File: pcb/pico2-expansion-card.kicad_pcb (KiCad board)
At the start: 2 copper layers, 26 x 30 mm, 39 parts, among them J3 Conn_01x04_Socket, J4 Conn_01x03_Socket, P1 USB_C_Plug_USB2.0, SW1 SW_Push, U2 RP2354A, U4 AP2127K-3.3, Y1 ABM8-272-T3

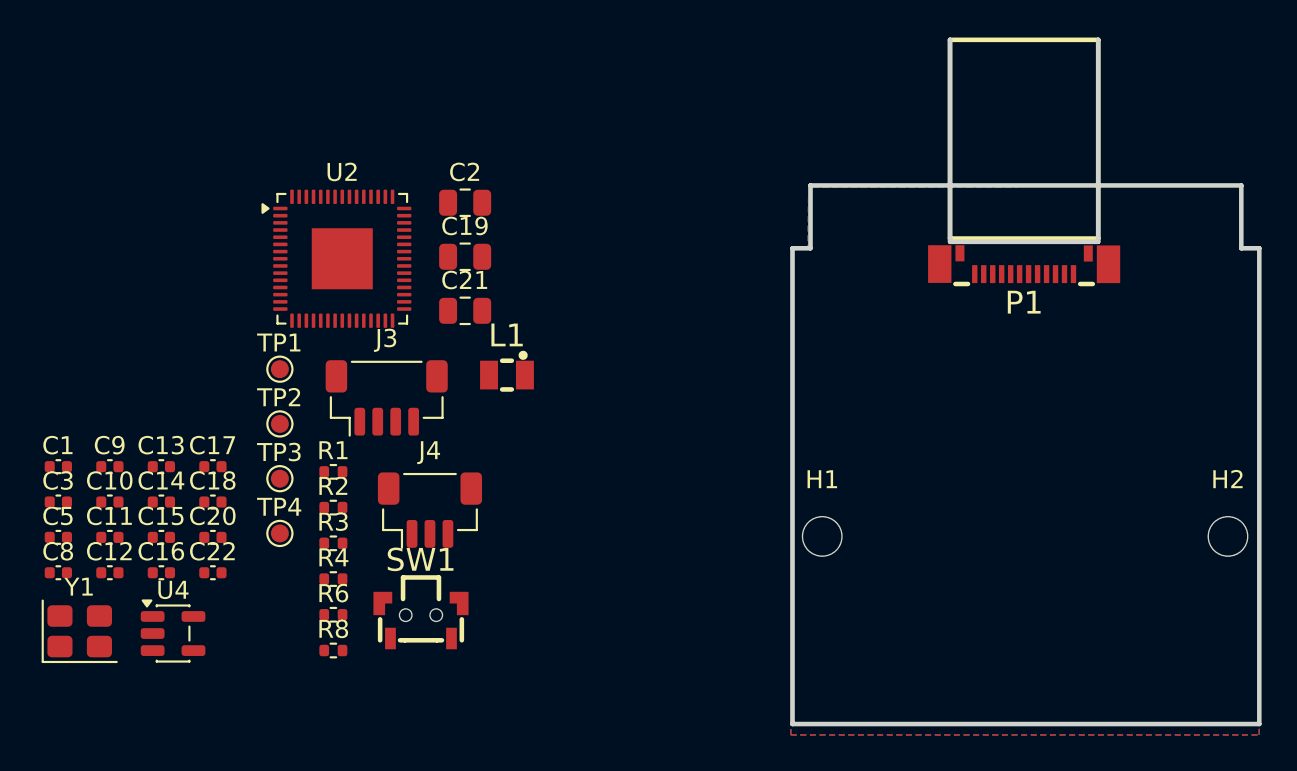
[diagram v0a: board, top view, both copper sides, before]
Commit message: edit schematic, change type-c, add single button bootsel reset, make pcb
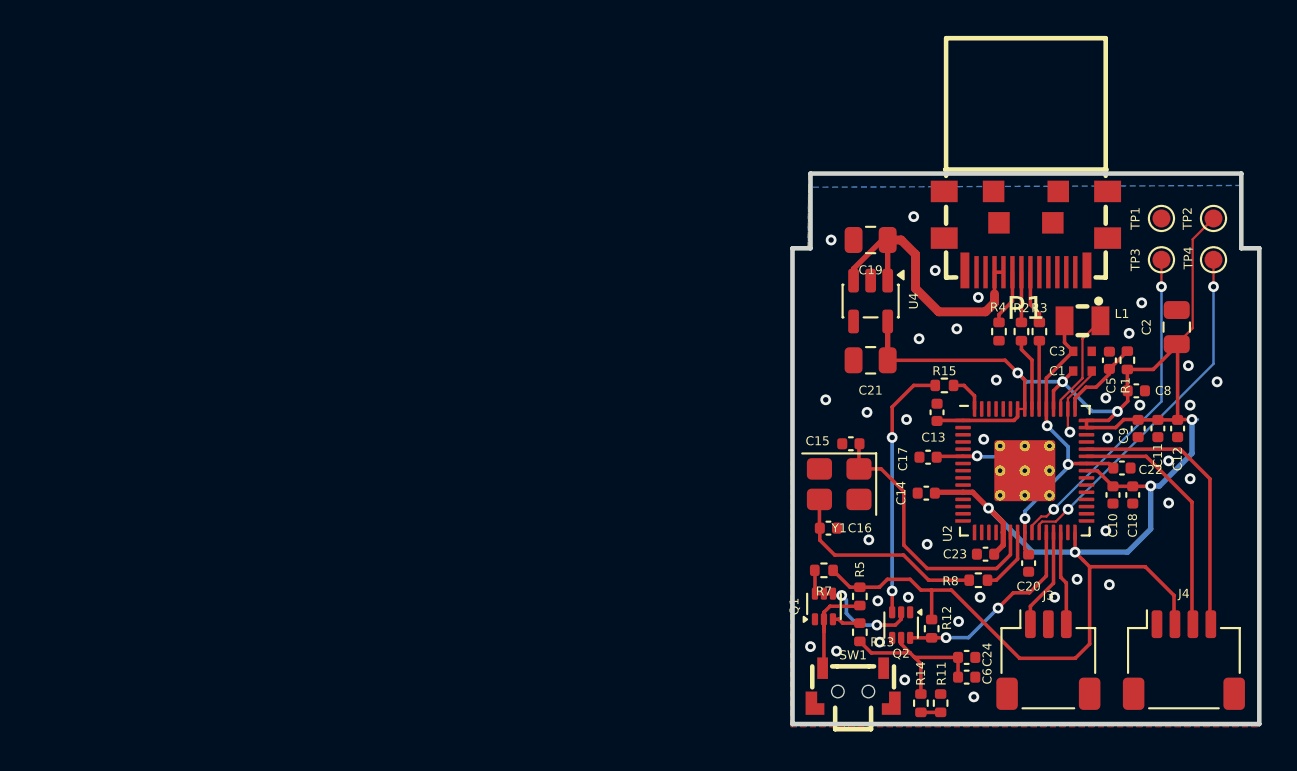
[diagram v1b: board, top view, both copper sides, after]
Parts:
- removed H1, H2: MountingHole, MountingHole:MountingHole_2.2mm_M2
- removed R6: 1k, Resistor_SMD:R_0402_1005Metric
- added C23: 100n, Capacitor_SMD:C_0402_1005Metric, F.Cu at (167.0, 91.5)
- added C24: 4u7, Capacitor_SMD:C_0402_1005Metric, F.Cu at (165.9, 97.2)
- added C6: 4u7, Capacitor_SMD:C_0402_1005Metric, F.Cu at (165.9, 98.3)
- added Q1: EM6K6, Package_TO_SOT_SMD:SOT-563, F.Cu at (158.0, 94.4)
- added Q2: EM6K6, Package_TO_SOT_SMD:SOT-563, F.Cu at (162.3, 95.5)
- added R11: 51K, Resistor_SMD:R_0402_1005Metric, F.Cu at (164.5, 99.8)
- added R12: 5K1, Resistor_SMD:R_0402_1005Metric, F.Cu at (164.0, 95.7)
- added R13: 51K, Resistor_SMD:R_0402_1005Metric, F.Cu at (160.0, 95.8)
- added R14: 51K, Resistor_SMD:R_0402_1005Metric, F.Cu at (163.4, 99.8)
- added R15: 1K, Resistor_SMD:R_0402_1005Metric, F.Cu at (164.7, 82.1)
- added R5: 5K1, Resistor_SMD:R_0402_1005Metric, F.Cu at (160.0, 93.8)
- added R7: 5K1, Resistor_SMD:R_0402_1005Metric, F.Cu at (158.0, 92.4)
- C1, C3: footprint Capacitor_SMD:C_0402_1005Metric -> pico2parts:C_0402_1005Metric_small_pads
- J3: renamed from J4; footprint Connector_JST:JST_SH_BM03B-SRSS-TB_1x03-1MP_P1.00mm_Vertical -> Connector_JST:JST_SH_SM03B-SRSS-TB_1x03-1MP_P1.00mm_Horizontal
- J4: renamed from J3; footprint Connector_JST:JST_SH_BM04B-SRSS-TB_1x04-1MP_P1.00mm_Vertical -> Connector_JST:JST_SH_SM04B-SRSS-TB_1x04-1MP_P1.00mm_Horizontal
- P1: value USB_C_Plug_USB2.0 -> ~; footprint pico2parts:USB-SMD_TC-002_1 -> pico2parts:USB-C-SMD_TYPE-C-31-G-10
- U2: footprint Package_DFN_QFN:QFN-60-1EP_7x7mm_P0.4mm_EP3.4x3.4mm -> pico2parts:RP2350-QFN-60-1EP_7x7_P0.4mm_EP3.4x3.4mm_ThermalVias
- moved C8 60.9 mm to (175.4, 82.4), turned to 180 degrees
- moved C12 60.0 mm to (177.7, 84.5), turned to 90 degrees
- moved C5 59.4 mm to (173.9, 80.7), turned to 90 degrees
- moved C11 58.7 mm to (176.6, 84.5), turned to 90 degrees
- moved C3 57.7 mm to (172.4, 80.2)
- moved C9 57.3 mm to (175.5, 84.5), turned to 90 degrees
- moved C1 57.3 mm to (172.4, 81.3)
- moved C10 55.9 mm to (174.1, 88.2), turned to 90 degrees
- moved TP4 54.2 mm to (179.7, 75.1), turned to 90 degrees
- moved TP2 53.2 mm to (179.7, 72.8), turned to 90 degrees
- moved C18 51.2 mm to (175.2, 88.2), turned to 90 degrees
- moved C22 51.0 mm to (174.6, 86.7)
- moved TP3 50.6 mm to (176.8, 75.1), turned to 90 degrees
- moved TP1 49.8 mm to (176.8, 72.8), turned to 90 degrees
- moved J4 46.7 mm to (178.1, 97.4)
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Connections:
- J3 pad 1: /GPIO4/TX -> /GPIO16/TX
- J3 pad 3: /GPIO5/RX -> /GPIO17/RX
- SW1 pad 2: /~{USB_BOOT} -> /SWITCH
- U2 pad 26: unconnected-(U2-RUN-Pad26) -> /nRST
- U2 pad 27: /GPIO16 -> /GPIO16/TX
- U2 pad 28: /GPIO17 -> /GPIO17/RX
- U2 pad 60: Net-(U2-~{QSPI_SS}) -> /~{USB_BOOT}
- U2 pad 7: /GPIO4/TX -> /GPIO4
- U2 pad 8: /GPIO5/RX -> /GPIO5
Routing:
- net +3.3V: track 0.00 -> 113.6 mm, vias 0 -> 7
- net +1V1: track 0.00 -> 25.8 mm, vias 0 -> 4
- net /SWDIO: track 0.00 -> 19.7 mm, vias 0 -> 2
- net /SWCLK: track 0.00 -> 18.4 mm, vias 0 -> 2
- net VBUS: track 0.00 -> 16.6 mm
- net /GPIO27/SCL: track 0.00 -> 15.7 mm
- net /XIN: track 0.00 -> 15.5 mm
- net Net-(Q2B-D): track 0.00 -> 14.3 mm, vias 0 -> 2
- net /GPIO26/SDA: track 0.00 -> 13.8 mm
- net Net-(C16-Pad1): track 0.00 -> 11.5 mm
- net /nRST: track 0.00 -> 11.4 mm, vias 0 -> 2
- net Net-(Q2B-G): track 0.00 -> 10.3 mm
- net Net-(Q1A-D): track 0.00 -> 7.94 mm, vias 0 -> 2
- net /SWITCH: track 0.00 -> 6.22 mm
- net /VREG_LX: track 0.00 -> 5.83 mm
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- added copper zone on B.Cu, net GND
- added copper zone on F.Cu, net GND
- removed copper zone on F.Cu, net +3.3V
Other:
- board size 26 x 30 mm -> 26 x 30.7 mm

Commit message: finish v0.1.0p prototype design
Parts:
- added H1: MountingHole, MountingHole:MountingHole_2.2mm_M2, F.Cu at (158.0, 82.1)
- added H1: MountingHole, MountingHole:MountingHole_2.2mm_M2, F.Cu at (180.4, 82.0)
- moved R13 4.22 mm to (164.0, 97.2)
- moved C21 2.91 mm to (163.4, 79.9), turned to -90 degrees
- moved R14 2.56 mm to (165.8, 98.9), turned to 0 degrees
- moved R5 1.95 mm to (160.0, 91.9), turned to 90 degrees
- moved R11 1.32 mm to (165.8, 100.0), turned to 180 degrees
- moved R12 0.96 mm to (164.7, 95.0)
- moved C24 0.72 mm to (165.8, 96.5)
- moved C6 0.72 mm to (165.8, 97.7)
- moved Q2 0.64 mm to (162.3, 94.8)
- moved C2 0.35 mm to (177.7, 78.5)
- moved C10 0.10 mm to (174.0, 88.2)
- moved C18 0.10 mm to (175.1, 88.2)
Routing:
- net +3.3V: track 113.6 -> 105.1 mm, vias 7 -> 8
- net Net-(Q1B-D): track 1.59 -> 6.62 mm
- net /SWITCH: track 6.22 -> 11.1 mm
- net Net-(Q2B-G): track 10.3 -> 8.13 mm
- net /XIN: track 15.5 -> 14.8 mm
- net Net-(Q2B-D): track 14.3 -> 13.7 mm
- net Net-(Q1A-D): track 7.94 -> 7.32 mm, vias 2 -> 0
- net /nRST: track 11.4 -> 11.1 mm, vias 2 -> 0
- net GND: vias 38 -> 32
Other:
- board size 26 x 30.7 mm -> 26 x 30.9 mm
- board text added: "License: CERN-OHL-S v2 Version: 0.1.0p (Prototype)"
- board text added: "PCB produced by:"
- board text added: "Pico2 Expansion Card"

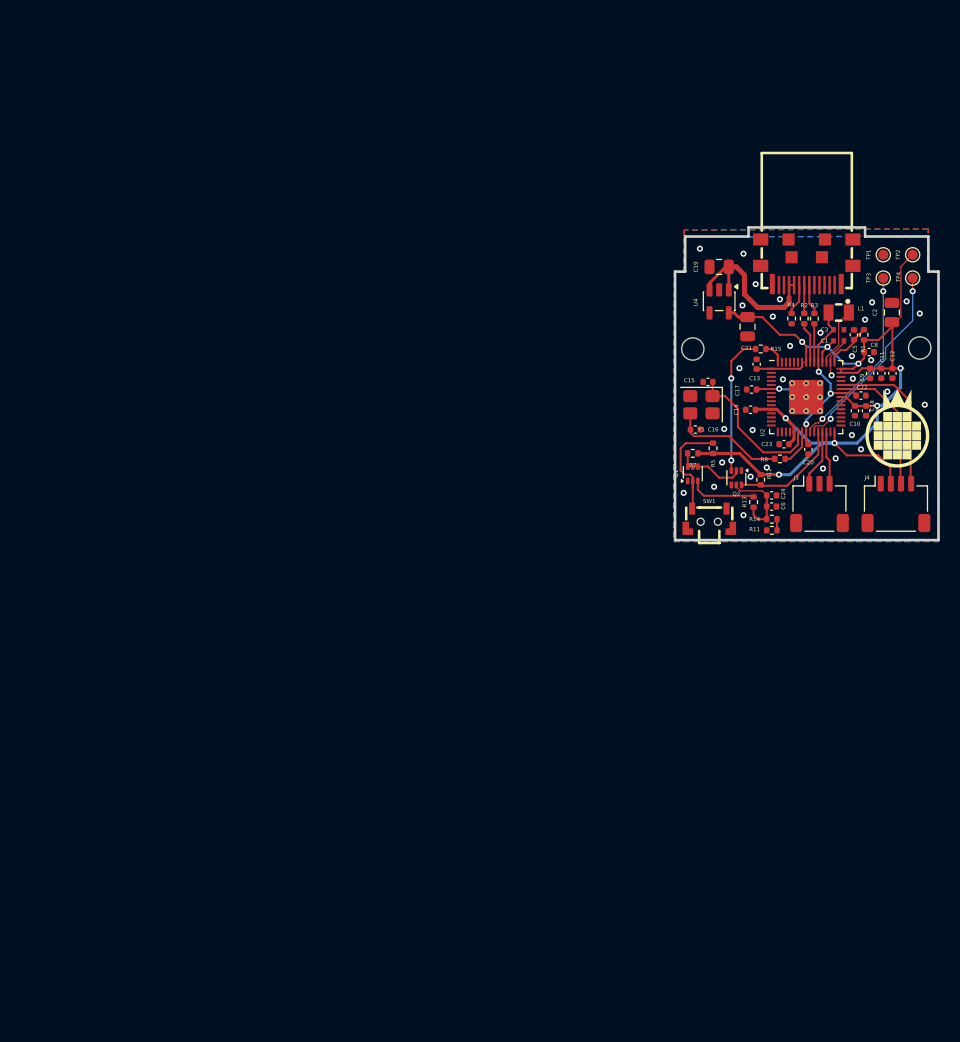
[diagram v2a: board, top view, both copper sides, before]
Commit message: minor cosmetic changes in schematics and footprints
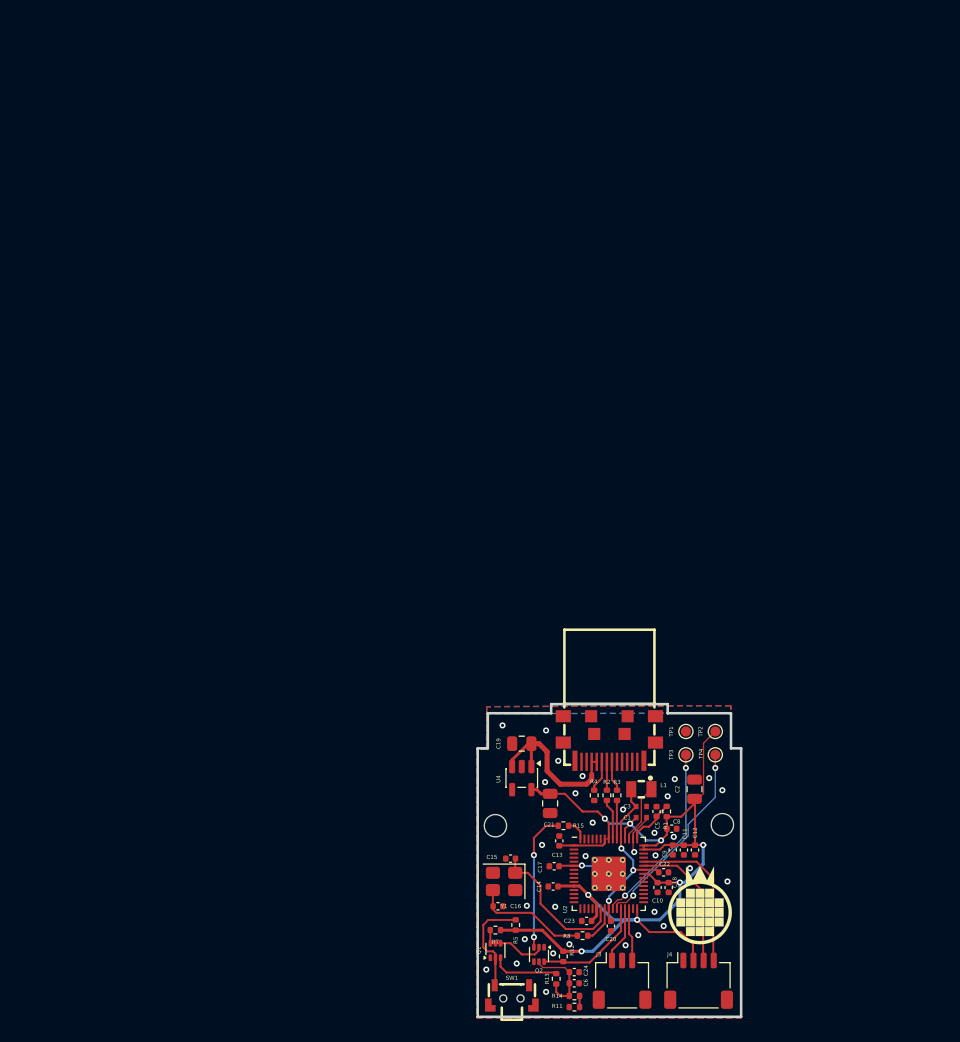
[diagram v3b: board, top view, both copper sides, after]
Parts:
- moved C13 50.9 mm to (144.8, 130.7)
- moved C17 50.9 mm to (144.3, 133.2)
- moved C20 50.9 mm to (149.9, 139.1)
- moved H1 50.9 mm to (160.9, 129.1)
- moved Q2 50.9 mm to (142.8, 141.9)
- moved R11 50.9 mm to (146.3, 147.1)
- moved R15 50.9 mm to (145.2, 129.2)
- moved TP3 50.9 mm to (157.3, 122.2)
- moved C11 50.9 mm to (157.1, 131.6)
- moved C12 50.9 mm to (158.2, 131.6)
- moved C14 50.9 mm to (144.2, 135.2)
- moved C15 50.9 mm to (140.0, 132.4)
- moved C23 50.9 mm to (147.5, 138.6)
- moved C9 50.9 mm to (156.0, 131.6)
- moved H1 50.9 mm to (138.5, 129.2)
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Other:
- board text added: "riscfruit.com"

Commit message: gerber and centroid
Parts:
- moved J3 0.06 mm to (151.0, 144.5)
- moved J4 0.06 mm to (158.6, 144.5)
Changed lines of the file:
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@@
 	(footprint "Connector_JST:JST_SH_SM03B-SRSS-TB_1x03-1MP_P1.00mm_Horizontal"
 		(layer "F.Cu")
-		(at 151.02 144.45)
+		(at 151.03 144.505)
 		(descr "JST SH series connector, SM03B-SRSS-TB (http://www.jst-mfg.com/product/pdf/eng/eSH.pdf)")
 		(tags "connector JST SH horizontal")
@@
 	(footprint "pico2parts:BUTTON-SW-SMD_2P-TS24CA"
 		(layer "F.Cu")
-		(at 140.145 145.875 180)
+		(at 140.145 145.905 180)
 		(property "Reference" "SW1"
 			(at 0.00005 1.7 0)
@@
 			(polygon
 				(pts
-					(xy 140.5516 144.8512) (xy 140.5506 145.0511) (xy 139.7504 145.0502) (xy 139.7497 144.8505) (xy 138.6497 144.8505)
-					(xy 138.6497 144.7505) (xy 138.2508 144.7503) (xy 138.2505 144.8501) (xy 137.8707 144.8476) (xy 137.8703 147.1494)
-					(xy 138.2484 147.1519) (xy 138.2691 147.3511) (xy 138.5301 147.3501) (xy 138.5505 147.15) (xy 139.0182 147.1525)
-					(xy 139.0067 148.427) (xy 141.2689 148.4272) (xy 141.2732 147.2288) (xy 142.4249 147.2263) (xy 142.4201 144.8498)
-					(xy 142.0499 144.8502) (xy 142.049 144.751) (xy 141.651 144.7509) (xy 141.6507 144.8502) (xy 140.551 144.851)
+					(xy 140.5516 144.8812) (xy 140.5506 145.0811) (xy 139.7504 145.0802) (xy 139.7497 144.8805) (xy 138.6497 144.8805)
+					(xy 138.6497 144.7805) (xy 138.2508 144.7803) (xy 138.2505 144.8801) (xy 137.8707 144.8776) (xy 137.8703 147.1794)
+					(xy 138.2484 147.1819) (xy 138.2691 147.3811) (xy 138.5301 147.3801) (xy 138.5505 147.18) (xy 139.0182 147.1825)
+					(xy 139.0067 148.457) (xy 141.2689 148.4572) (xy 141.2732 147.2588) (xy 142.4249 147.2563) (xy 142.4201 144.8798)
+					(xy 142.0499 144.8802) (xy 142.049 144.781) (xy 141.651 144.7809) (xy 141.6507 144.8802) (xy 140.551 144.881)
 				)
 			)
@@
 			(polygon
 				(pts
-					(xy 138.2702 144.75) (xy 138.6202 144.75) (xy 138.6202 145.5) (xy 138.2702 145.5)
+					(xy 138.2702 144.78) (xy 138.6202 144.78) (xy 138.6202 145.53) (xy 138.2702 145.53)
 				)
 			)
@@
 			(polygon
 				(pts
-					(xy 141.6702 144.75) (xy 142.0202 144.75) (xy 142.0202 145.5) (xy 141.6702 145.5)
+					(xy 141.6702 144.78) (xy 142.0202 144.78) (xy 142.0202 145.53) (xy 141.6702 145.53)
 				)
 			)
@@
 			(polygon
 				(pts
-					(xy 137.87 146.15) (xy 137.87 147.15) (xy 138.5451 147.15) (xy 138.5451 147.04) (xy 137.9801 147.04)
-					(xy 137.9801 146.15)
+					(xy 137.87 146.18) (xy 137.87 147.18) (xy 138.5451 147.18) (xy 138.5451 147.07) (xy 137.9801 147.07)
+					(xy 137.9801 146.18)
 				)
 			)
@@
 			(polygon
 				(pts
-					(xy 142.4204 146.15) (xy 142.4204 147.15) (xy 141.7454 147.15) (xy 141.7454 147.04) (xy 142.3103 147.04)
-					(xy 142.3103 146.15)
+					(xy 142.4204 146.18) (xy 142.4204 147.18) (xy 141.7454 147.18) (xy 141.7454 147.07) (xy 142.3103 147.07)
+					(xy 142.3103 146.18)
 				)
 			)
@@
 	(footprint "Connector_JST:JST_SH_SM04B-SRSS-TB_1x04-1MP_P1.00mm_Horizontal"
 		(layer "F.Cu")
-		(at 158.57 144.45)
+		(at 158.57 144.505)
 		(descr "JST SH series connector, SM04B-SRSS-TB (http://www.jst-mfg.com/product/pdf/eng/eSH.pdf)")
 		(tags "connector JST SH horizontal")

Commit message: cosmetic changes
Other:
- board text added: "BUTTON"
- board text added: "I2C"
- board text added: "UART"

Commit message: cosmetic minor changes
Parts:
- moved C10 74.9 mm to (109.7, 75.2)
- moved C11 74.9 mm to (112.3, 71.5)
- moved C15 74.9 mm to (95.2, 72.4)
- moved C16 74.9 mm to (93.9, 77.1)
- moved C18 74.9 mm to (110.8, 75.2)
- moved C22 74.9 mm to (110.3, 73.7)
- moved C23 74.9 mm to (102.7, 78.5)
- moved C24 74.9 mm to (101.5, 83.6)
- moved C6 74.9 mm to (101.5, 84.7)
- moved C9 74.9 mm to (111.2, 71.5)
- moved H1 74.9 mm to (93.7, 69.1)
- moved Q1 74.9 mm to (93.7, 81.4)
- moved R13 74.9 mm to (99.7, 84.2)
- moved R2 74.9 mm to (104.7, 66.1)
- moved R3 74.9 mm to (105.7, 66.1)
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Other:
- board size 26 x 30.9 mm -> 26 x 30.6 mm

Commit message: fix connections
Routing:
- net GND: track 4.04 -> 7.01 mm
- net +3.3V: track 105.1 -> 106.9 mm
- net VBUS: track 16.6 -> 18.0 mm
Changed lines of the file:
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@@
+	)
+	(segment
+		(start 102.2 64.2)
+		(end 102.18745 64.18745)
+		(width 0.127)
+		(layer "F.Cu")
+		(net "GND")
+	)
+	(segment
+		(start 102.18745 64.18745)
+		(end 102.18745 62.8185)
+		(width 0.127)
+		(layer "F.Cu")
+		(net "GND")
+	)
+	(segment
+		(start 102.68755 63.71245)
+		(end 102.2 64.2)
+		(width 0.127)
+		(layer "F.Cu")
+		(net "GND")
 	)
 	(segment
@@
 	)
 	(segment
+		(start 102.68755 62.8185)
+		(end 102.68755 63.71245)
+		(width 0.127)
+		(layer "F.Cu")
+		(net "GND")
+	)
+	(segment
 		(start 107.275 70.4375)
 		(end 107.275 69.858526)
@@
 	)
 	(via
-		(at 102.2875 64.225)
+		(at 102.2 64.2)
 		(size 0.6)
 		(drill 0.3)
@@
 	)
 	(segment
+		(start 110.00625 70.64375)
+		(end 110.3875 71.025)
+		(width 0.2)
+		(layer "F.Cu")
+		(net "+3.3V")
+	)
+	(segment
 		(start 108.9175 73.975)
 		(end 109.6875 74.745)
@@
 	)
 	(segment
-		(start 104.482977 68.429523)
-		(end 104.875 68.821545)
-		(width 0.2)
-		(layer "F.Cu")
-		(net "+3.3V")
-	)
-	(segment
 		(start 94.2075 79.435)
 		(end 94.1975 79.425)
@@
 	)
 	(segment
-		(start 104.875 70.4375)
-		(end 104.475 70.4375)
-		(width 0.127)
-		(layer "F.Cu")
-		(net "+3.3V")
-	)
-	(segment
 		(start 108.9175 73.875)
 		(end 108.9175 73.975)
@@
 	)
 	(segment
-		(start 104.875 68.821545)
-		(end 104.875 70.4375)
+		(start 104.875 70.4375)
+		(end 104.875 68.875)
 		(width 0.2)
 		(layer "F.Cu")
@@
 	)
 	(segment
+		(start 110.00625 70.60625)
+		(end 110.00625 70.64375)
+		(width 0.2)
+		(layer "F.Cu")
+		(net "+3.3V")
+	)
+	(segment
+		(start 104.482977 68.482977)
+		(end 104.482977 68.429523)
+		(width 0.2)
+		(layer "F.Cu")
+		(net "+3.3V")
+	)
+	(segment
 		(start 98.3075 79.435)
 		(end 100.3875 81.515)
@@
 	)
 	(segment
+		(start 110.0375 70.575)
+		(end 110.00625 70.60625)
+		(width 0.2)
+		(layer "F.Cu")
+		(net "+3.3V")
+	)
+	(segment
 		(start 103.675 78.0175)
 		(end 103.675 77.3125)
@@
 	)
 	(segment
+		(start 104.475 68.4375)
+		(end 104.482977 68.429523)
+		(width 0.2)
+		(layer "F.Cu")
+		(net "+3.3V")
+	)
+	(segment
 		(start 98.19375 65.975)
 		(end 97.78125 65.5625)
@@
 	)
 	(segment
+		(start 104.475 70.4375)
+		(end 104.475 68.4375)
+		(width 0.2)
+		(layer "F.Cu")
+		(net "+3.3V")
+	)
+	(segment
+		(start 104.875 68.875)
+		(end 104.482977 68.482977)
+		(width 0.2)
+		(layer "F.Cu")
+		(net "+3.3V")
+	)
+	(segment
 		(start 108.3125 73.875)
 		(end 108.9175 73.875)
@@
 		(start 107.5725 68.325)
 		(end 106.98 68.9175)
-		(width 0.2)
-		(layer "F.Cu")
-		(net "+3.3V")
-	)
-	(segment
-		(start 108.3125 71.475)
-		(end 108.3125 71.075)
 		(width 0.2)
 		(layer "F.Cu")
@@
 	)
 	(segment
+		(start 103.68755 62.8185)
+		(end 103.68755 64.02495)
+		(width 0.2)
+		(layer "F.Cu")
+		(net "VBUS")
+	)
+	(segment
+		(start 103.68755 64.02495)
+		(end 103.1875 64.525)
+		(width 0.2)
+		(layer "F.Cu")
+		(net "VBUS")
+	)
+	(segment
 		(start 96.937501 61.025)
 		(end 95.3375 62.625001)
@@
 		(end 96.937501 61.025)
 		(width 0.3)
-		(layer "F.Cu")
-		(net "VBUS")
-	)
-	(segment
-		(start 103.68755 62.8185)
-		(end 103.18745 62.8185)
-		(width 0.2)
 		(layer "F.Cu")
 		(net "VBUS")
@@
 	)
 	(zone
+		(layer "F.Cu")
+		(hatch edge 0.5)
+		(connect_pads
+			(clearance 0)
+		)
+		(min_thickness 0.25)
+		(keepout
+			(tracks not_allowed)
+			(vias not_allowed)
+			(pads not_allowed)
+			(copperpour not_allowed)
+			(footprints allowed)
+		)
+		(placement
+			(enabled no)
+			(sheetname "")
+		)
+		(fill
+			(thermal_gap 0.5)
+			(thermal_bridge_width 0.5)
+			(island_removal_mode 0)
+		)
+		(polygon
+			(pts
+				(xy 100.4 57.4) (xy 109.4 57.4) (xy 109.4 63.2) (xy 100.4 63.2)
+			)
+		)
+	)
+	(zone
